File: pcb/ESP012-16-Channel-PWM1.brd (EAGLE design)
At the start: 77.5 x 71.1 mm, 27 parts, among them IC2 UA78M33DCY, J1 DCJ0202, Q1 IRLML2244TRPBF, Q2 IRLML2244TRPBF, Q3 IRLML2244TRPBF, Q4 IRLML2244TRPBF, Q5 IRLML2244TRPBF, Q6 IRLML2244TRPBF, Q7 IRLML2244TRPBF, Q8 IRLML2244TRPBF

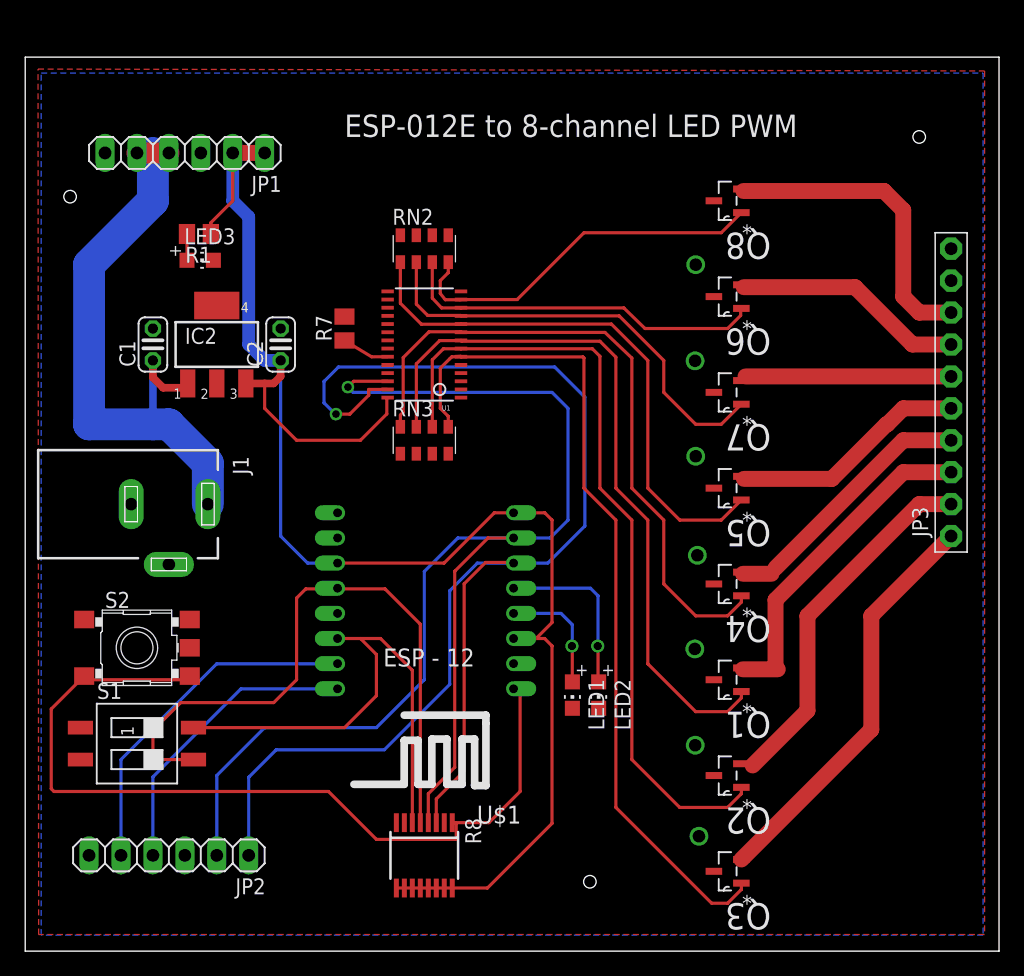
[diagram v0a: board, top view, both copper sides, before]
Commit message: changed 12V supply for LEDs to thicker wire
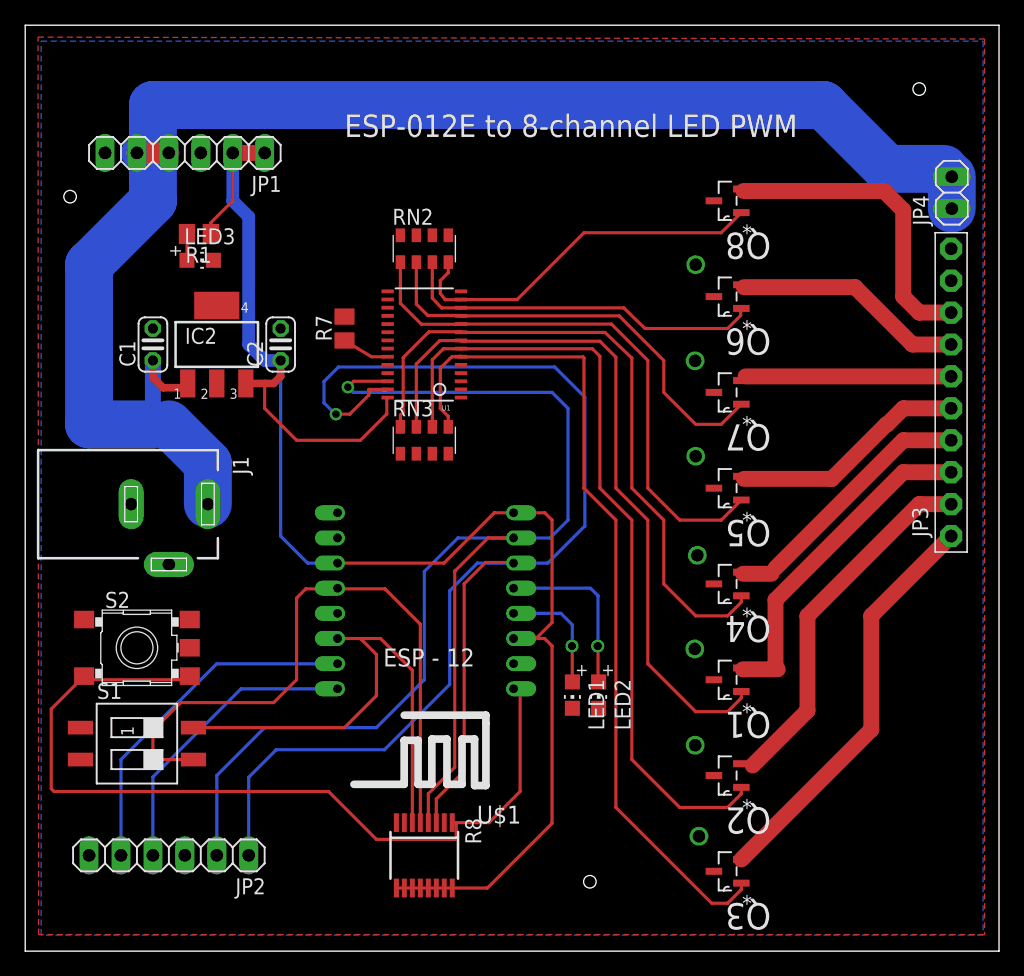
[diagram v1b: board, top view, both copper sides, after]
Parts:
- added JP4: (no value), pinhead:1X02
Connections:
- net VCC12: now also JP4.1, JP4.2
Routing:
- net VCC12: track 49.9 -> 123.4 mm
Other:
- board size 77.5 x 71.1 mm -> 77.5 x 73.7 mm
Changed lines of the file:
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@@
 <grid distance="0.05" unitdist="inch" unit="mm" style="lines" multiple="1" display="no" altdistance="0.05" altunitdist="mm" altunit="mm"/>
 <layers>
-<layer number="1" name="Top" color="4" fill="1" visible="yes" active="yes"/>
-<layer number="16" name="Bottom" color="1" fill="1" visible="no" active="yes"/>
+<layer number="1" name="Top" color="4" fill="1" visible="no" active="yes"/>
+<layer number="16" name="Bottom" color="1" fill="1" visible="yes" active="yes"/>
 <layer number="17" name="Pads" color="2" fill="1" visible="yes" active="yes"/>
 <layer number="18" name="Vias" color="2" fill="1" visible="yes" active="yes"/>
@@
 <layer number="42" name="bRestrict" color="1" fill="10" visible="no" active="yes"/>
 <layer number="43" name="vRestrict" color="2" fill="10" visible="no" active="yes"/>
-<layer number="44" name="Drills" color="7" fill="1" visible="no" active="yes"/>
-<layer number="45" name="Holes" color="7" fill="1" visible="no" active="yes"/>
+<layer number="44" name="Drills" color="7" fill="1" visible="yes" active="yes"/>
+<layer number="45" name="Holes" color="7" fill="1" visible="yes" active="yes"/>
 <layer number="46" name="Milling" color="3" fill="1" visible="no" active="yes"/>
 <layer number="47" name="Measures" color="7" fill="1" visible="no" active="yes"/>
@@
 <layer number="113" name="ReferenceLS" color="7" fill="1" visible="no" active="no"/>
 <layer number="114" name="IDFDebug" color="4" fill="1" visible="no" active="yes"/>
-<layer number="116" name="centerDrill" color="9" fill="4" visible="yes" active="yes"/>
+<layer number="116" name="centerDrill" color="9" fill="4" visible="no" active="yes"/>
 <layer number="118" name="Rect_Pads" color="7" fill="1" visible="no" active="no"/>
 <layer number="121" name="_tsilk" color="7" fill="1" visible="no" active="yes"/>
@@
 <wire x1="-1.2" y1="5.45" x2="-1.2" y2="76" width="0.01" layer="114"/>
 <wire x1="-1.2" y1="76" x2="76" y2="76.15" width="0.01" layer="114"/>
-<wire x1="-1.27" y1="76.2" x2="76.2" y2="76.2" width="0.01" layer="20"/>
-<wire x1="76.2" y1="76.2" x2="76.2" y2="5.08" width="0.01" layer="20"/>
+<wire x1="-1.27" y1="78.74" x2="76.2" y2="78.74" width="0.01" layer="20"/>
+<wire x1="76.2" y1="78.74" x2="76.2" y2="5.08" width="0.01" layer="20"/>
 <wire x1="76.2" y1="5.08" x2="-1.27" y2="5.08" width="0.01" layer="20"/>
-<wire x1="-1.27" y1="5.08" x2="-1.27" y2="76.2" width="0.01" layer="20"/>
+<wire x1="-1.27" y1="5.08" x2="-1.27" y2="78.74" width="0.01" layer="20"/>
 <text x="24.13" y="69.85" size="1.778" layer="21">ESP-012E to 8-channel LED PWM</text>
 <hole x="2.3" y="65.1" drill="1"/>
-<hole x="69.85" y="69.85" drill="1"/>
+<hole x="69.85" y="73.66" drill="1"/>
 <hole x="43.65" y="10.6" drill="1"/>
 <circle x="2.3" y="65.1" radius="0.4" width="0.3" layer="116"/>
@@
 <element name="LED3" library="adafruit" package="CHIP-LED0805" value="" x="12.65" y="60.04" rot="R270"/>
 <element name="R1" library="adafruit" package="M2012" value="5K" x="12.55" y="62.13" rot="R180"/>
+<element name="JP4" library="pinhead" package="1X02" value="" x="72.44" y="65.42" rot="R90"/>
 </elements>
 <signals>
@@
 <contactref element="RN3" pad="1"/>
 <polygon width="0.8128" layer="16" isolate="0.4064">
-<vertex x="74.93" y="74.93"/>
+<vertex x="74.93" y="77.47"/>
 <vertex x="74.93" y="6.35"/>
 <vertex x="0" y="6.35"/>
-<vertex x="0" y="74.93"/>
+<vertex x="0" y="77.47"/>
 </polygon>
 <via x="52.02" y="52.04" extent="1-16" drill="1" shape="square"/>
@@
 <via x="52.33" y="14.22" extent="1-16" drill="1" shape="square"/>
 <polygon width="0.6096" layer="1" isolate="0.4064">
-<vertex x="-0.25" y="75.25"/>
-<vertex x="75.05" y="75.1"/>
+<vertex x="-0.25" y="77.79"/>
+<vertex x="75.05" y="77.64"/>
 <vertex x="75.05" y="6.4"/>
 <vertex x="-0.2" y="6.4"/>
@@
 <contactref element="JP1" pad="5"/>
 <wire x1="7.62" y1="68.58" x2="10.16" y2="68.58" width="1.6764" layer="1"/>
-<wire x1="13.26" y1="40.64" x2="13.26" y2="43.89" width="2.54" layer="16"/>
-<wire x1="13.26" y1="43.89" x2="10.16" y2="46.99" width="2.54" layer="16"/>
+<wire x1="13.26" y1="40.64" x2="13.26" y2="43.89" width="3.81" layer="16"/>
+<wire x1="13.26" y1="43.89" x2="10.16" y2="46.99" width="3.81" layer="16"/>
 <wire x1="10.16" y1="46.99" x2="8.89" y2="46.99" width="2.54" layer="16"/>
-<wire x1="8.89" y1="46.99" x2="3.81" y2="46.99" width="2.54" layer="16"/>
-<wire x1="3.81" y1="46.99" x2="3.81" y2="59.69" width="2.54" layer="16"/>
-<wire x1="3.81" y1="59.69" x2="8.89" y2="64.77" width="2.54" layer="16"/>
-<wire x1="8.89" y1="64.77" x2="8.89" y2="68.58" width="2.54" layer="16"/>
-<wire x1="8.89" y1="52.07" x2="8.89" y2="46.99" width="0.6096" layer="16"/>
+<wire x1="8.89" y1="46.99" x2="3.81" y2="46.99" width="3.81" layer="16"/>
+<wire x1="3.81" y1="46.99" x2="3.81" y2="59.69" width="3.81" layer="16"/>
+<wire x1="3.81" y1="59.69" x2="8.89" y2="64.77" width="3.81" layer="16"/>
+<wire x1="8.89" y1="64.77" x2="8.89" y2="68.58" width="3.81" layer="16"/>
+<wire x1="8.89" y1="52.07" x2="8.89" y2="46.99" width="1.27" layer="16"/>
 <wire x1="8.89" y1="52.07" x2="8.89" y2="50.71" width="0.6096" layer="1"/>
 <wire x1="8.89" y1="50.71" x2="9.7" y2="49.9" width="0.6096" layer="1"/>
 <wire x1="9.7" y1="49.9" x2="11.3174" y2="49.9" width="0.6096" layer="1"/>
 <wire x1="11.3174" y1="49.9" x2="11.6586" y2="50.2412" width="0.6096" layer="1"/>
-<wire x1="8.89" y1="68.58" x2="10.16" y2="68.58" width="0" layer="19" extent="16-16"/>
+<contactref element="JP4" pad="2"/>
+<contactref element="JP4" pad="1"/>
+<wire x1="7.62" y1="68.58" x2="8.89" y2="68.58" width="2.54" layer="16"/>
+<wire x1="8.89" y1="68.58" x2="8.89" y2="72.39" width="3.81" layer="16"/>
+<wire x1="8.89" y1="72.39" x2="62.23" y2="72.39" width="3.81" layer="16"/>
+<wire x1="62.23" y1="72.39" x2="67.31" y2="67.31" width="3.81" layer="16"/>
+<wire x1="67.31" y1="67.31" x2="71.82" y2="67.31" width="3.81" layer="16"/>
+<wire x1="71.82" y1="67.31" x2="72.44" y2="66.69" width="2.54" layer="16"/>
+<wire x1="72.44" y1="66.69" x2="72.44" y2="64.15" width="3.81" layer="16"/>
 </signal>
 <signal name="TX">
